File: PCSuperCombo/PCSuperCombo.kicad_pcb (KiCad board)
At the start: 2 copper layers, 127 x 106.7 mm, 23 parts, among them J1 IDE to CF adapter, J2 CF Adapter Power, J3 Bus_ISA_8bit, SW1 Options, U1 BIOS FLASH, U2 74HCT245, U3 ATF/GAL16V8x-15, U4 DS1315, Y1 32.768 KHz

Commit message: PCSuperCombo: Early WIP.
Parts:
- added C7: 0.1uF, Capacitor_SMD:C_1206_3216Metric, F.Cu at (232.4, 112.4)
- added C8: 10uf 16v, Capacitor_Tantalum_SMD:CP_EIA-3216-18_Kemet-A, F.Cu at (251.5, 144.8)
- added C9: 10uf 16v, Capacitor_Tantalum_SMD:CP_EIA-3216-18_Kemet-A, F.Cu at (177.2, 120.0)
- added R4: 10K, Resistor_SMD:R_1206_3216Metric, F.Cu at (270.6, 68.6)
- added R5: 10K, Resistor_SMD:R_1206_3216Metric, F.Cu at (276.2, 68.6)
- added R6: 10K, Resistor_SMD:R_1206_3216Metric, F.Cu at (270.6, 71.9)
- added R7: 10K, Resistor_SMD:R_1206_3216Metric, F.Cu at (270.6, 75.2)
- added R8: 10K, Resistor_SMD:R_1206_3216Metric, F.Cu at (276.2, 73.0)
- added U5: AS6C1/4008-55PCN, Package_DIP:DIP-32_W15.24mm_Socket, F.Cu at (219.5, 65.3)
- added U6: AS6C1/4008-55PCN, Package_DIP:DIP-32_W15.24mm_Socket, F.Cu at (239.1, 65.8)
- added U7: ATF/GAL16V8x-15, Package_DIP:DIP-24_W7.62mm_Socket, F.Cu at (219.9, 112.8)
- C6: value 22-44uF 16-25v -> 0.1uF; footprint Capacitor_Tantalum_SMD:CP_EIA-3528-15_AVX-H -> Capacitor_SMD:C_1206_3216Metric
- J1: value IDE to CF adapter -> IDE_CONNECTOR
- SW1: value Options -> SW_DIP_x10; footprint Button_Switch_THT:SW_DIP_SPSTx04_Slide_9.78x12.34mm_W7.62mm_P2.54mm -> Button_Switch_THT:SW_DIP_SPSTx10_Slide_9.78x27.58mm_W7.62mm_P2.54mm
- moved R3 179.6 mm to (281.8, 65.3)
- moved R2 174.0 mm to (276.2, 65.3)
- moved R1 168.4 mm to (270.6, 65.3)
- moved SW1 160.0 mm to (266.1, 66.7)
- moved Y1 157.4 mm to (250.2, 154.9)
- moved C4 153.2 mm to (246.4, 132.7)
- moved C1 152.2 mm to (251.5, 118.7)
- moved C6 147.8 mm to (248.3, 109.9)
- moved C3 144.0 mm to (237.5, 121.3)
- moved C2 113.4 mm to (233.7, 129.5)
- moved U2 107.0 mm to (190.5, 178.4)
- moved U3 107.0 mm to (157.5, 178.4)
- moved U4 107.0 mm to (172.7, 158.1)
- moved U1 54.9 mm to (111.1, 169.5)
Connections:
- J1 pad 25: ~IOR -> ~IOR~_DELAYED
- J3 pad 42: AEN -> Net-(J3-Pad42)
- J3 pad 8: Net-(J3-Pad8) -> ~CARD_SEL_ISA
- R1 pad 2: ROM_ADDR_JUMPER -> BASE_RAM_0
- R2 pad 2: ATA_ADDR_JUMPER -> BASE_RAM_1
- R3 pad 2: V20_JUMPER -> BASE_RAM_2
- SW1 pad 4: ~CE~_BIOS_DECODE -> GND
- SW1 pad 5: ~CE~_BIOS_THRU -> GND
- SW1 pad 6: V20_JUMPER -> GND
- SW1 pad 7: ATA_ADDR_JUMPER -> GND
- SW1 pad 8: ROM_ADDR_JUMPER -> GND
- U1 pad 13: D0 -> D0_BUF
- U1 pad 14: D1 -> D1_BUF
- U1 pad 15: D2 -> D2_BUF
- U1 pad 17: D3 -> D3_BUF
- U1 pad 18: D4 -> D4_BUF
- U1 pad 19: D5 -> D5_BUF
- U1 pad 20: D6 -> D6_BUF
- U1 pad 21: D7 -> D7_BUF
- U1 pad 22: ~CE~_BIOS_THRU -> ~CE~_BIOS
- U1 pad 24: ~MEMR -> ~MEMR~_DELAYED
- U2 pad 1: ~IOR -> ~IOR_OR_MEMR
- U2 pad 19: ~CS1~_ATA -> GND
- U3 pad 1: A16 -> A04
- U3 pad 11: A19 -> A17
- U3 pad 12: A17 -> ~MEMR~_DELAYED
- U3 pad 13: A05 -> ~MEMR
- U3 pad 17: AEN -> ~IOR
- U3 pad 18: ROM_ADDR_JUMPER -> ATA_ADDR_JUMPER
- U3 pad 19: ATA_ADDR_JUMPER -> ROM_ADDR_JUMPER
- U3 pad 2: A18 -> A05
- U3 pad 3: A15 -> A06
- U3 pad 4: A06 -> A07
- U3 pad 5: A07 -> A08
- U3 pad 6: A08 -> A09
- U3 pad 7: A09 -> RESET
- U3 pad 8: A04 -> A15
- U3 pad 9: RESET -> A16
- U4 pad 12: ~MEMR -> ~MEMR~_DELAYED
- U4 pad 7: D0 -> D0_BUF
- Y1 pad 1: /XTAL2 -> /XTAL1
- Y1 pad 2: /XTAL1 -> /XTAL2
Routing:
- net GND: track 501.1 -> 153.0 mm, vias 101 -> 18
- net A02: track 167.1 -> 0.00 mm, vias 4 -> 0
- net A01: track 156.1 -> 0.00 mm, vias 3 -> 0
- net A03: track 155.2 -> 0.00 mm, vias 2 -> 0
- net A00: track 133.0 -> 0.00 mm, vias 4 -> 0
- net ~MEMR: track 116.7 -> 0.00 mm, vias 3 -> 0
- net ~IOR: track 108.2 -> 0.00 mm, vias 4 -> 0
- net RESET: track 102.7 -> 0.00 mm, vias 3 -> 0
- net D0: track 101.2 -> 0.00 mm, vias 1 -> 0
- net AEN: track 94.3 -> 0.00 mm, vias 3 -> 0
- net D7: track 87.6 -> 0.00 mm, vias 1 -> 0
- net A16: track 87.3 -> 0.00 mm, vias 1 -> 0
- net A18: track 87.2 -> 0.00 mm, vias 1 -> 0
- net D6: track 85.3 -> 0.00 mm, vias 1 -> 0
- net ~CE~_BIOS_THRU: track 85.1 -> 0.00 mm, vias 1 -> 0
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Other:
- board text added: "PC SUPER COMBO"
- board text added: "Packages: R1-R3: 1206 C1-C7: 1206 C8, C9: 3218"
- board text removed: "22-33uF 16-25v 3528 package"
- board text removed: "CF SUPER-LITE"
- board text removed: "R1-R3 & C1-C5 are 1206 package"

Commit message: PCSuperCombo: Early layout work.
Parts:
- added C8: 0.1uF, Capacitor_SMD:C_1206_3216Metric, F.Cu at (76.8, 60.3)
- U7: footprint Package_DIP:DIP-24_W7.62mm_Socket -> Package_DIP:DIP-20_W7.62mm_Socket
- moved R1 188.4 mm to (83.9, 39.9)
- moved R3 188.4 mm to (95.1, 39.9)
- moved R4 188.4 mm to (83.9, 43.2)
- moved R2 188.4 mm to (89.5, 39.9)
- moved R5 188.4 mm to (89.5, 43.2)
- moved R8 179.0 mm to (100.3, 40.0)
- moved R6 177.7 mm to (95.2, 43.2)
- moved C6 176.5 mm to (81.7, 51.4), turned to 180 degrees
- moved R7 173.3 mm to (100.3, 43.2)
- moved U6 171.1 mm to (77.5, 121.9), turned to 90 degrees
- moved C9 170.2 mm to (81.9, 129.5)
- moved C2 159.0 mm to (76.8, 103.5), turned to 0 degrees
- moved C7 158.5 mm to (76.8, 81.9)
- moved Y1 147.0 mm to (122.6, 81.9), turned to 0 degrees
- moved U5 146.3 mm to (77.5, 100.3), turned to 90 degrees
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- renumbered C9 to C10, C8 to C9
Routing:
- net GND: track 153.0 -> 809.2 mm, vias 18 -> 34
- net VCC: track 375.4 -> 494.0 mm, vias 6 -> 5
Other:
- board size 127 x 106.7 mm -> 123.3 x 95 mm
- board text added: "Packages: R1-R3: 1206 C1-C8: 1206 C9,C10: 3218"
- board text removed: "Lowest possible edge - no need to use."
- board text removed: "Packages: R1-R3: 1206 C1-C7: 1206 C8, C9: 3218"

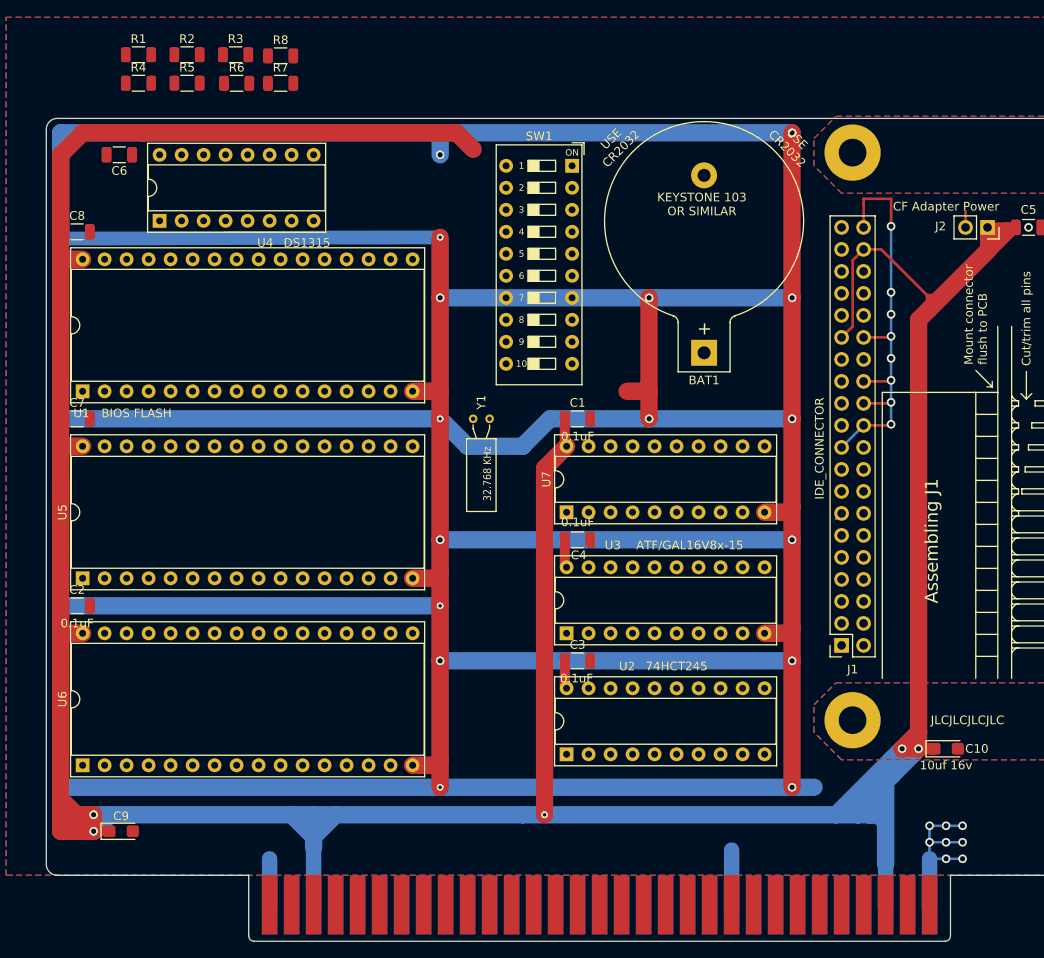
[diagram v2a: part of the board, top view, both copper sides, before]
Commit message: PCSuperCombo: Some layout experiments. Schematic needs to be completed before proceeding further.
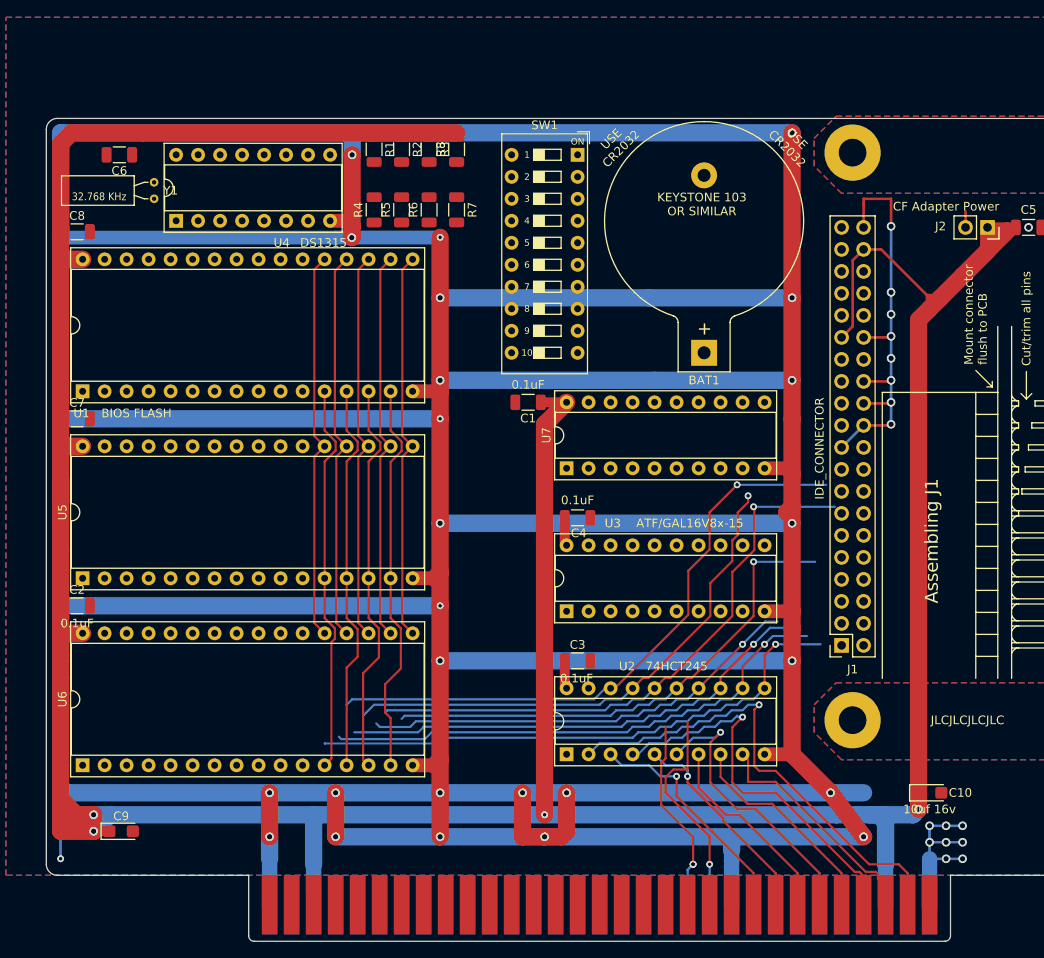
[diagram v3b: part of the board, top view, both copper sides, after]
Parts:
- moved Y1 45.8 mm to (85.7, 54.6), turned to 270 degrees
- moved R4 30.9 mm to (111.1, 57.8), turned to 90 degrees
- moved R1 29.3 mm to (111.1, 50.8), turned to 270 degrees
- moved R5 28.8 mm to (114.3, 57.8), turned to 90 degrees
- moved R2 27.1 mm to (114.3, 50.8), turned to 270 degrees
- moved R6 26.6 mm to (117.5, 57.8), turned to 90 degrees
- moved R7 25.0 mm to (120.7, 57.8), turned to 270 degrees
- moved R3 24.9 mm to (117.5, 50.8), turned to 270 degrees
- moved R8 23.0 mm to (120.7, 50.8), turned to 90 degrees
- moved C1 6.02 mm to (128.9, 80.0), turned to 180 degrees
- moved C10 5.43 mm to (175.3, 125.1)
- moved U7 5.08 mm to (133.3, 87.6)
- moved C4 2.54 mm to (134.6, 93.3)
- moved U3 2.54 mm to (133.3, 104.1)
- moved U4 1.91 mm to (88.3, 59.1)
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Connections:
- net Net-(J3-Pad7) renamed -12V
- net Net-(J3-Pad9) renamed +12V
- U2 pad 2: D0 -> D7
- U2 pad 3: D1 -> D0
- U2 pad 4: D2 -> D5
- U2 pad 5: D3 -> D1
- U2 pad 6: D4 -> D3
- U2 pad 7: D5 -> D2
- U2 pad 8: D6 -> D4
- U2 pad 9: D7 -> D6
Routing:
- net D0_BUF: track 0.00 -> 116.7 mm, vias 0 -> 1
- net GND: track 809.2 -> 923.0 mm, vias 34 -> 45
- net D2_BUF: track 0.90 -> 113.5 mm, vias 0 -> 1
- net D7_BUF: track 0.00 -> 109.4 mm, vias 0 -> 1
- net D1_BUF: track 0.00 -> 107.1 mm, vias 0 -> 1
- net D6_BUF: track 0.00 -> 105.9 mm, vias 0 -> 1
- net D3_BUF: track 0.18 -> 104.3 mm, vias 0 -> 1
- net D5_BUF: track 0.00 -> 101.6 mm, vias 0 -> 1
- net D4_BUF: track 0.00 -> 96.7 mm, vias 0 -> 1
- net D7: track 0.00 -> 55.8 mm, vias 0 -> 1
- net D5: track 0.00 -> 45.6 mm, vias 0 -> 1
- net A00: track 0.00 -> 45.2 mm
- net D3: track 0.00 -> 33.0 mm, vias 0 -> 1
- net VCC: track 494.0 -> 465.0 mm, vias 5 -> 4
- net D0: track 0.00 -> 27.2 mm, vias 0 -> 1
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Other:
- net class Default: trace_width 0.3 -> 0.25
- net class Power: trace_width 0.5 -> 0.25

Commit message: PCSuperCombo: Complete glue connectons to GAL's. Add circuit for LED drive.
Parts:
- added J4: LED, Connector_PinHeader_2.54mm:PinHeader_1x02_P2.54mm_Horizontal, F.Cu at (191.8, 127.0)
- added R10: 180R, Resistor_SMD:R_1206_3216Metric, F.Cu at (189.6, 131.0)
- added R9: 180R, Resistor_SMD:R_1206_3216Metric, F.Cu at (184.0, 131.0)
- moved C10 6.38 mm to (175.9, 118.7)
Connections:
- J1 pad 39: Net-(J1-Pad39) -> ~DASP~_ATA
- J3 pad 42: Net-(J3-Pad42) -> AEN
- SW1 pad 9: ~CE~_BIOS_DECODE -> ~CE~_BIOS
- U1 pad 22: ~CE~_BIOS -> ~CE~_BIOS_THRU
- U3 pad 1: A04 -> BASE_RAM_0
- U3 pad 11: A17 -> A19
- U3 pad 12: ~MEMR~_DELAYED -> RESET
- U3 pad 13: ~MEMR -> ~CS~_RAM1
- U3 pad 14: ~CE~_BIOS_DECODE -> ~CS~_RAM0
- U3 pad 15: ~CS1~_ATA -> MEM_DECODED
- U3 pad 16: ~RESET -> ~CE~_BIOS
- U3 pad 17: ~IOR -> ~RESET
- U3 pad 18: ATA_ADDR_JUMPER -> /PTERMS_SPARE
- U3 pad 2: A05 -> BASE_RAM_1
- U3 pad 3: A06 -> BASE_RAM_2
- U3 pad 4: A07 -> UMB_ENABLE
- U3 pad 5: A08 -> UBM_SIZE
- U3 pad 6: A09 -> A15
- U3 pad 7: RESET -> A16
- U3 pad 8: A15 -> A17
- U3 pad 9: A16 -> A18
- U4 pad 11: ~CE~_BIOS_DECODE -> ~CE~_BIOS
- U5 pad 22: A19 -> ~CS~_RAM0
- U6 pad 22: A19 -> ~CS~_RAM1
- U7 pad 1: Net-(U7-Pad1) -> ATA_ADDR_JUMPER
- U7 pad 11: Net-(U7-Pad11) -> ~DASP~_ATA
- U7 pad 12: Net-(U7-Pad12) -> ~IOR~_DELAYED
- U7 pad 13: Net-(U7-Pad13) -> ~IOR_OR_MEMR
- U7 pad 14: Net-(U7-Pad14) -> ~MEMR~_DELAYED
- U7 pad 15: Net-(U7-Pad15) -> ~CARD_SEL
- U7 pad 16: Net-(U7-Pad16) -> ~CS1~_ATA
- U7 pad 17: Net-(U7-Pad17) -> LED_DRIVE
- U7 pad 18: Net-(U7-Pad18) -> ~MEMR
- U7 pad 19: Net-(U7-Pad19) -> ~IOR
- U7 pad 2: Net-(U7-Pad2) -> A04
- U7 pad 3: Net-(U7-Pad3) -> A05
- U7 pad 4: Net-(U7-Pad4) -> A06
- U7 pad 5: Net-(U7-Pad5) -> A07
- U7 pad 6: Net-(U7-Pad6) -> A08
- U7 pad 7: Net-(U7-Pad7) -> A09
- U7 pad 8: Net-(U7-Pad8) -> AEN
- U7 pad 9: Net-(U7-Pad9) -> MEM_DECODED

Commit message: PCSuperCombo: Shuffle some GAL logic around so now there is enough room in the logic to add a single UART jumper / decode.
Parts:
- added R9: 10K, Resistor_SMD:R_1206_3216Metric, F.Cu at (111.8, 43.2)
- SW1: value SW_DIP_x10 -> Options
- renumbered R9 to R11
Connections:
- J3 pad 8: ~CARD_SEL_ISA -> ~CARD_SEL
- R4 pad 2: UMB_ENABLE -> UMB_SIZE_0
- R5 pad 2: UBM_SIZE -> UMB_SIZE_1
- R8 pad 2: V20_JUMPER -> COM1_ENABLE
- SW1 pad 10: ~CARD_SEL -> Net-(SW1-Pad10)
- SW1 pad 11: ~CARD_SEL_ISA -> ~CE~_BIOS
- SW1 pad 12: ~CE~_BIOS_THRU -> ~IOR_OR_MEMR
- SW1 pad 13: V20_JUMPER -> ~CARD_SEL
- SW1 pad 14: ATA_ADDR_JUMPER -> ~CE~_BIOS_THRU
- SW1 pad 15: ROM_ADDR_JUMPER -> Net-(SW1-Pad15)
- SW1 pad 16: UBM_SIZE -> V20_JUMPER
- SW1 pad 17: UMB_ENABLE -> COM1_ENABLE
- SW1 pad 18: BASE_RAM_2 -> ATA_ADDR_JUMPER
- SW1 pad 19: BASE_RAM_1 -> ROM_ADDR_JUMPER
- SW1 pad 20: BASE_RAM_0 -> UMB_SIZE_1
- SW1 pad 9: ~CE~_BIOS -> GND
- U3 pad 12: RESET -> ~IOR_OR_MEMR
- U3 pad 15: MEM_DECODED -> IO_DECODED
- U3 pad 17: ~RESET -> ~MEMR~_DELAYED
- U3 pad 18: /PTERMS_SPARE -> ~IOR~_DELAYED
- U3 pad 4: UMB_ENABLE -> UMB_SIZE_0
- U3 pad 5: UBM_SIZE -> UMB_SIZE_1
- U7 pad 12: ~IOR~_DELAYED -> IO_DECODED
- U7 pad 13: ~IOR_OR_MEMR -> ~CS~_COM1
- U7 pad 14: ~MEMR~_DELAYED -> RESET
- U7 pad 15: ~CARD_SEL -> ~RESET
- U7 pad 9: MEM_DECODED -> COM1_ENABLE

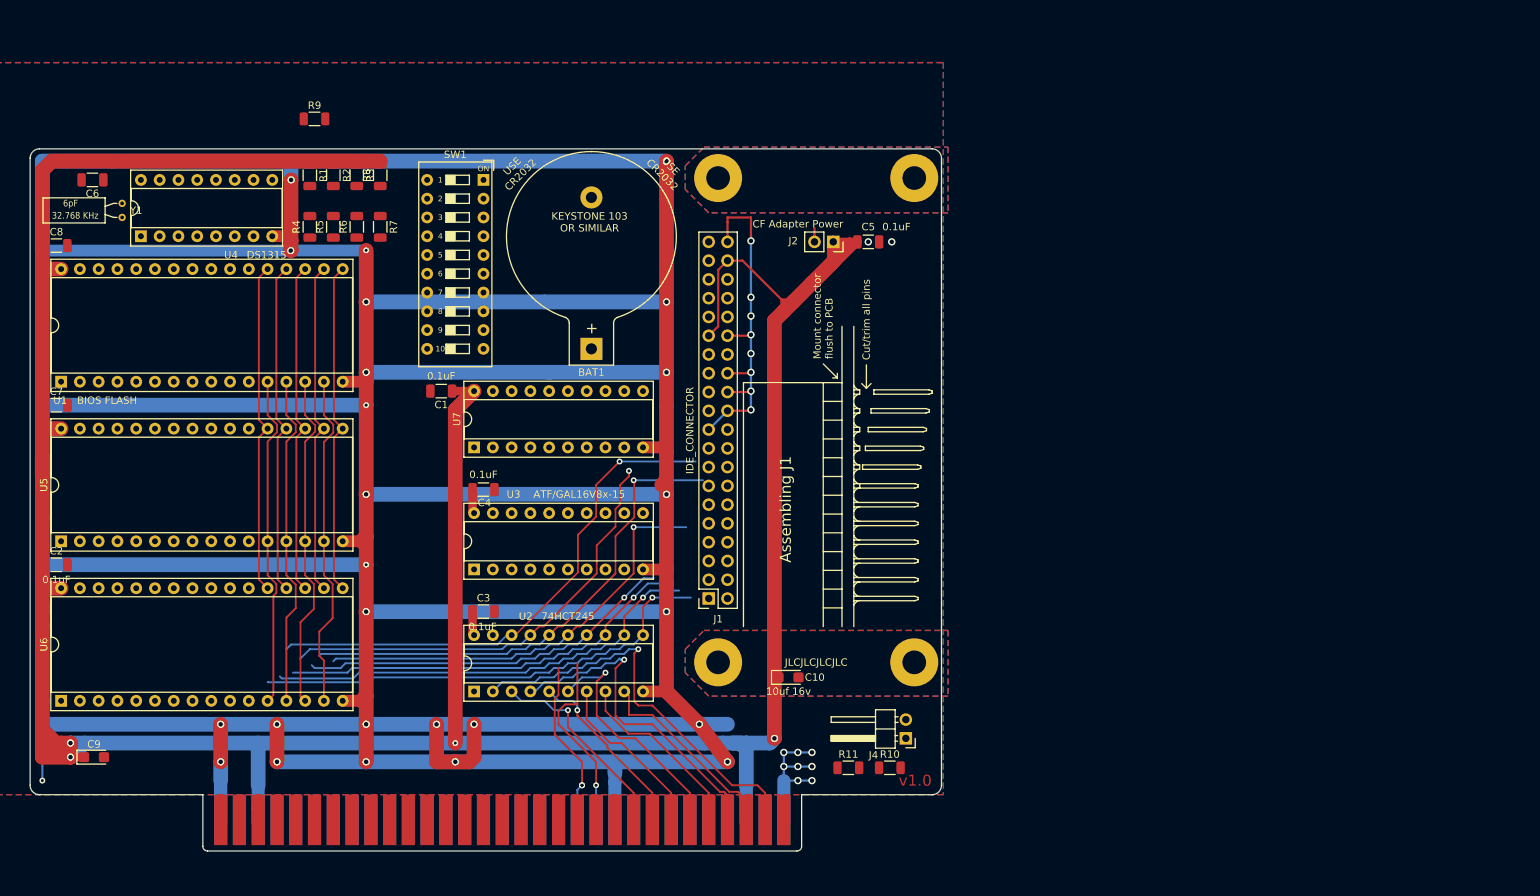
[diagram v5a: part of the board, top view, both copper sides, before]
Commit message: Initial work on addiing serial to PCSuperCombo.
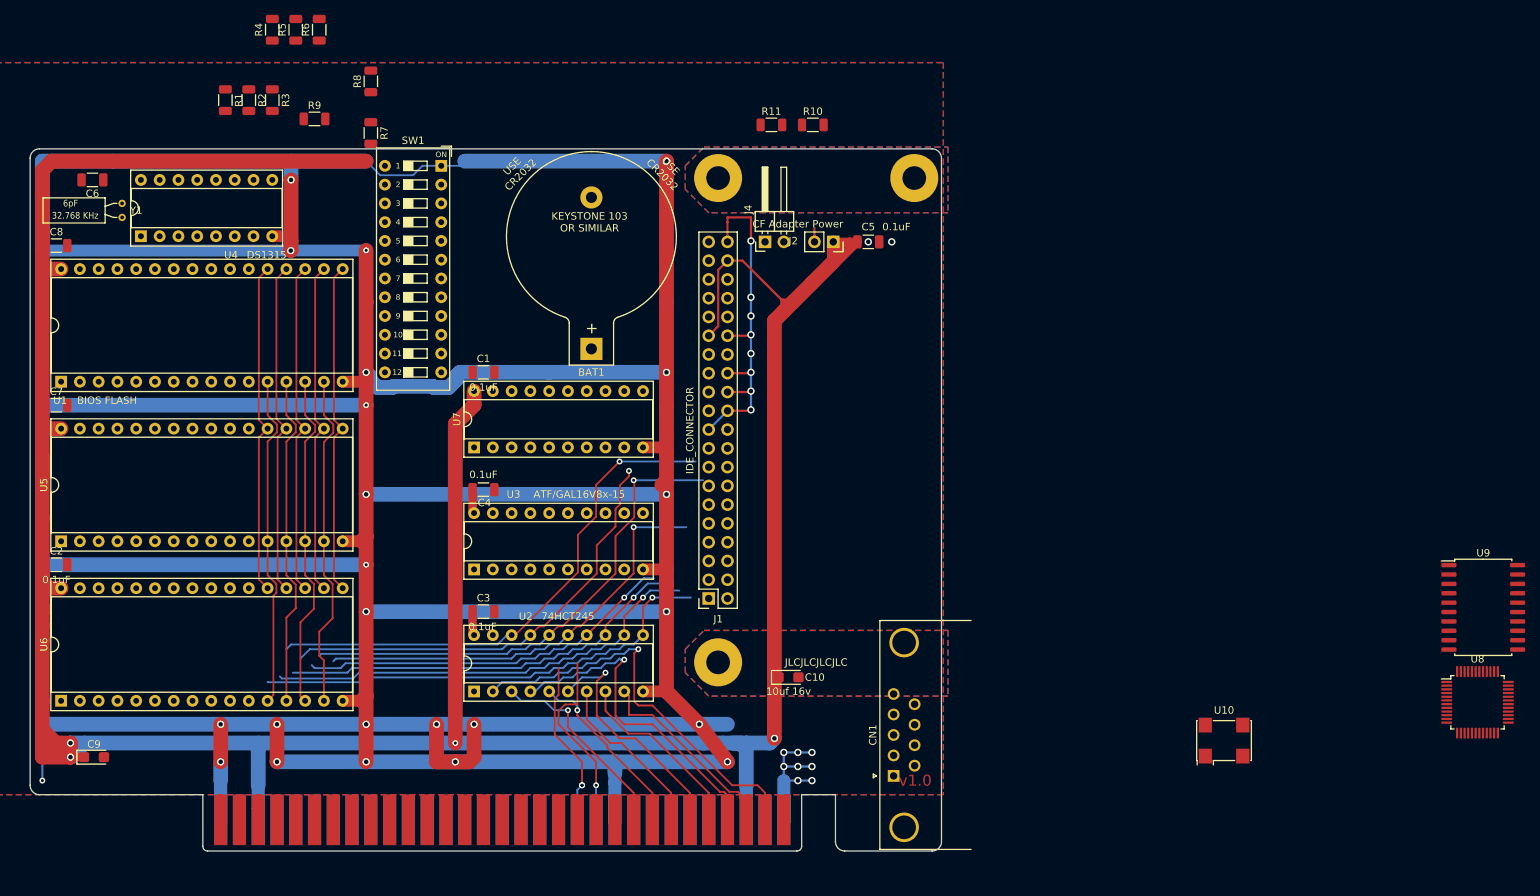
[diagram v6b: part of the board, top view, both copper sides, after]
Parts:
- removed H4: MountingHole_Pad, MountingHole:MountingHole_3.5mm_Pad
- added CN1: DB9 Male, Connector_Dsub:DSUB-9_Male_Horizontal_P2.77x2.84mm_EdgePinOffset7.70mm_Housed_MountingHolesOffset9.12mm, F.Cu at (190.1, 132.1)
- added U10: 1.8432 MHz, Oscillator:Oscillator_SMD_SeikoEpson_SG8002CA-4Pin_7.0x5.0mm, F.Cu at (234.8, 127.3)
- added U8: 16C550, Package_QFP:LQFP-48_7x7mm_P0.5mm, F.Cu at (269.1, 122.1)
- added U9: GD75232, Package_SO:SOIC-20W_7.5x12.8mm_P1.27mm, F.Cu at (269.9, 109.3)
- SW1: footprint Button_Switch_THT:SW_DIP_SPSTx10_Slide_9.78x27.58mm_W7.62mm_P2.54mm -> 00Custom:SW_DIP_SPSTx12
- moved R11 87.6 mm to (173.6, 44.0)
- moved R10 87.6 mm to (179.2, 44.0)
- moved J4 69.8 mm to (172.7, 59.8), turned to 90 degrees
- moved R4 27.1 mm to (106.0, 31.1)
- moved R5 27.1 mm to (109.2, 31.1)
- moved R6 27.1 mm to (112.4, 31.1)
- moved R1 15.3 mm to (99.7, 40.6)
- moved R2 15.3 mm to (102.9, 40.6)
- moved R3 15.3 mm to (106.0, 40.6)
- moved R7 12.8 mm to (119.4, 45.1)
- moved R8 12.8 mm to (119.4, 38.1)
- moved C1 6.25 mm to (134.6, 77.5), turned to 0 degrees
- moved SW1 6.02 mm to (128.9, 49.5)
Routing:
- net GND: track 923.0 -> 886.4 mm, vias 45 -> 43
- net VCC: track 465.0 -> 460.1 mm
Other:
- outline, holes or cut-outs redrawn
